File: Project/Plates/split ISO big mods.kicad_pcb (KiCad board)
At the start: 2 copper layers, 257.2 x 76.2 mm, 46 parts

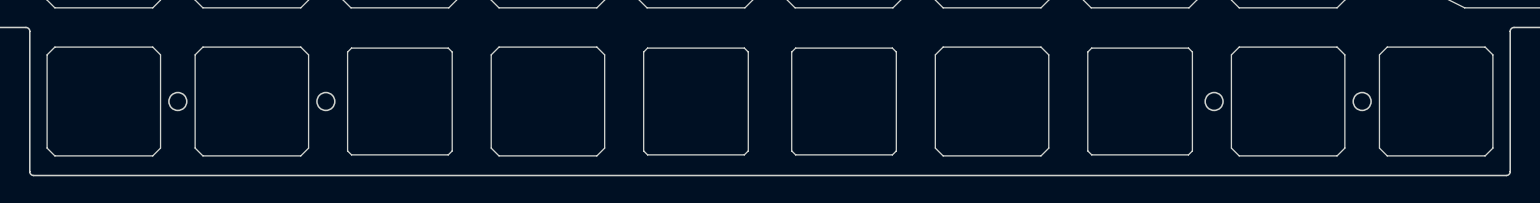
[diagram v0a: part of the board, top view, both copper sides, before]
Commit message: bottom row change, plate update, firmware update
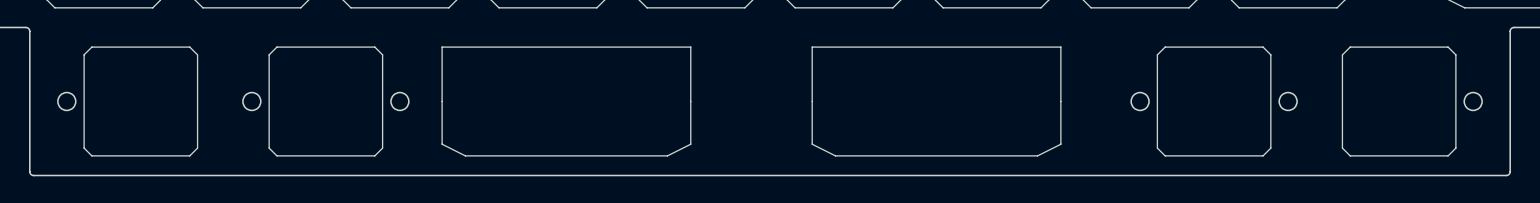
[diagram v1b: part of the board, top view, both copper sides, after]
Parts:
- removed the REF** at (212.7, 91.3)
- removed the REF** at (174.6, 91.3) (x2)
- removed the REF** at (79.4, 91.3)
- removed the REF** at (117.5, 91.3) (x2)
- removed the REF** at (60.3, 91.3)
- removed the REF** at (231.8, 91.3)
- added REF**: Value, cipulot_parts:ecs_plate_cut_1U, F.Cu at (227.0, 91.3)
- added REF**: Value, cipulot_parts:ecs_plate_cut_1U, F.Cu at (203.2, 91.3)
- added REF**: Value, cipulot_parts:ecs_plate_cut_2U, F.Cu at (119.9, 91.3)
- added REF**: Value, cipulot_parts:ecs_plate_cut_1U, F.Cu at (88.9, 91.3)
- added REF**: Value, cipulot_parts:ecs_plate_cut_1U, F.Cu at (65.1, 91.3)
- added REF**: Value, cipulot_parts:ecs_plate_cut_2U, F.Cu at (167.5, 91.3)
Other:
- outline, holes or cut-outs redrawn
